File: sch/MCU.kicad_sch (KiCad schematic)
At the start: 32 parts, among them J1 DE9_Pins_MountingHoles, J2 2x7P Pitch:1.27mm, SW1 TS-1087S-01526, U1 STM32G474CBT6, Y1 16MHz

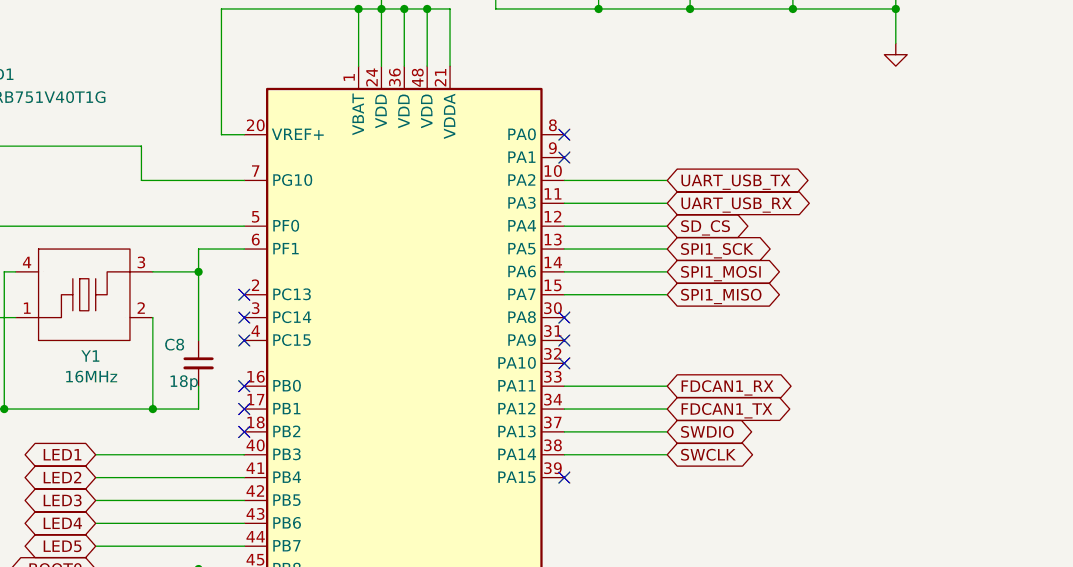
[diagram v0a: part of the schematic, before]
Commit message: Fix SPI pins add 3.3v led
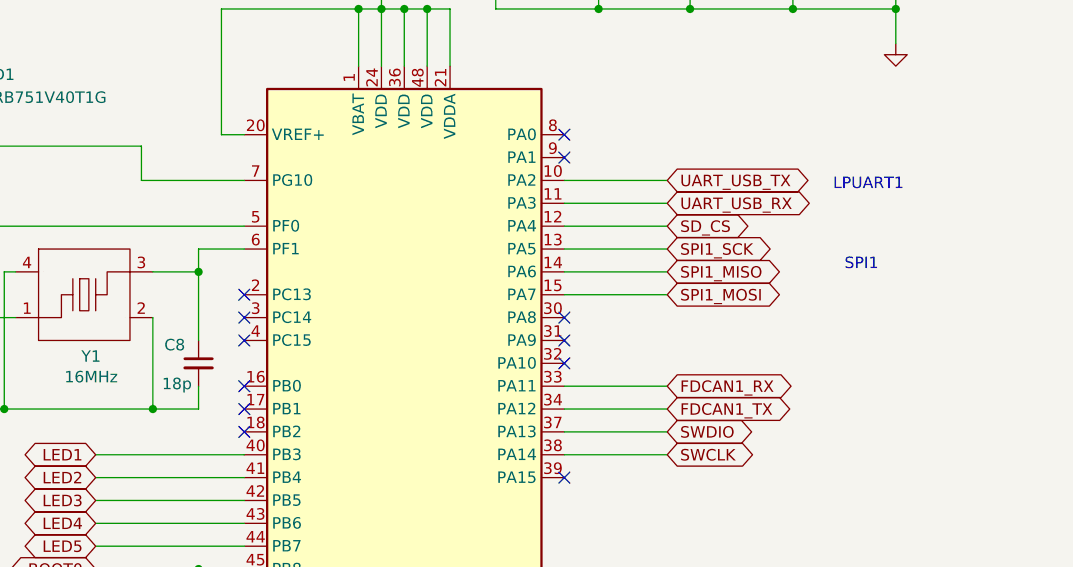
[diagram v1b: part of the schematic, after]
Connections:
- net SPI1_MISO: now also U1.14 (PA6); no longer U1.15 (PA7)
- net SPI1_MOSI: now also U1.15 (PA7); no longer U1.14 (PA6)
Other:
- note added: "LPUART1"
- note added: "SPI1"
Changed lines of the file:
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@@
 		)
 	)
+	(text "LPUART1"
+		(exclude_from_sim no)
+		(at 149.352 56.388 0)
+		(effects
+			(font
+				(size 1.27 1.27)
+			)
+		)
+	)
 	(text "max 120ma"
 		(exclude_from_sim no)
@@
 		)
 	)
+	(text "SPI1"
+		(exclude_from_sim no)
+		(at 148.59 65.278 0)
+		(effects
+			(font
+				(size 1.27 1.27)
+			)
+		)
+	)
 	(junction
 		(at 39.37 39.37)
@@
 	(global_label "SPI1_MISO"
 		(shape bidirectional)
-		(at 127 68.58 0)
+		(at 127 66.04 0)
 		(fields_autoplaced yes)
 		(effects
@@
 		)
 		(property "Intersheetrefs" "${INTERSHEET_REFS}"
-			(at 140.9541 68.58 0)
+			(at 140.9541 66.04 0)
 			(effects
 				(font
@@
 	(global_label "SPI1_MOSI"
 		(shape bidirectional)
-		(at 127 66.04 0)
+		(at 127 68.58 0)
 		(fields_autoplaced yes)
 		(effects
@@
 		)
 		(property "Intersheetrefs" "${INTERSHEET_REFS}"
-			(at 140.9541 66.04 0)
+			(at 140.9541 68.58 0)
 			(effects
 				(font
@@
 		)
 		(property "Value" "18p"
-			(at 71.628 78.232 0)
+			(at 70.866 78.486 0)
 			(effects
 				(font

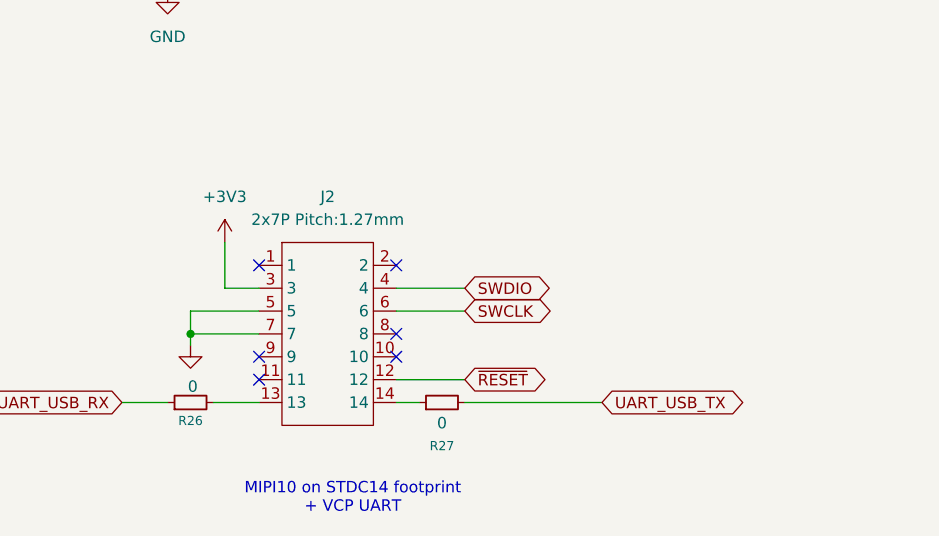
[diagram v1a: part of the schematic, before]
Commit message: change 2x22u to 3x10u plot all order jlcpcb + lcsc
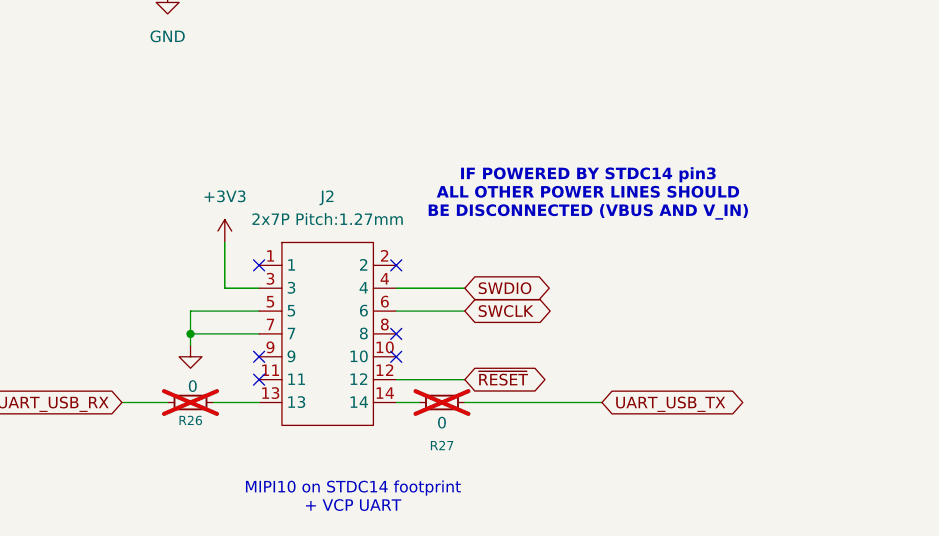
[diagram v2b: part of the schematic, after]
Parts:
- R26, R27: now not fitted
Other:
- note added: "IF POWERED BY STDC14 pin3 ALL OTHER POWER LINES SHOULD BE DISCONNECTED (VBUS AND V_IN)"
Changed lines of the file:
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@@
+		)
+	)
+	(text "IF POWERED BY STDC14 pin3\nALL OTHER POWER LINES SHOULD \nBE DISCONNECTED (VBUS AND V_IN)"
+		(exclude_from_sim no)
+		(at 144.526 152.146 0)
+		(effects
+			(font
+				(size 1.27 1.27)
+				(thickness 0.254)
+				(bold yes)
+			)
 		)
 	)
@@
 		(in_bom yes)
 		(on_board yes)
-		(dnp no)
+		(dnp yes)
 		(property "Reference" "R27"
 			(at 128.27 180.086 90)
@@
 		(in_bom yes)
 		(on_board yes)
-		(dnp no)
+		(dnp yes)
 		(property "Reference" "R26"
 			(at 100.33 177.292 90)
